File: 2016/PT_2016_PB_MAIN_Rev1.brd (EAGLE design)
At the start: 150.9 x 201.9 mm, 137 parts, among them M1+ ANDERSON_POWERPOLEPP45_PCB_HO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, M1- ANDERSON_POWERPOLEPP45_PCB_HO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, M2+ ANDERSON_POWERPOLEPP45_PCB_HO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, M2- ANDERSON_POWERPOLEPP45_PCB_HO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, M3+ ANDERSON_POWERPOLEPP45_PCB_HO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, M3- ANDERSON_POWERPOLEPP45_PCB_HO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, M4+ ANDERSON_POWERPOLEPP45_PCB_HO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, M4- ANDERSON_POWERPOLEPP45_PCB_HO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, M5+ ANDERSON_POWERPOLEPP45_PCB_HO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, M5- ANDERSON_POWERPOLEPP45_PCB_HO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, M6+ ANDERSON_POWERPOLEPP45_PCB_HO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, M6- ANDERSON_POWERPOLEPP45_PCB_HO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, Q1 Q_IRFS7437PbF, Q11 Q_IRFS7437PbF, Q12 2N7002, Q14 Q_IRFS7437PbF, Q16 Q_IRFS7437PbF, Q2 2N7002, Q20 Q_IRFS7437PbF, Q6 Q_IRFS7437PbF, Q7 Q_IRFS7437PbF, Q9 Q_IRFS7437PbF

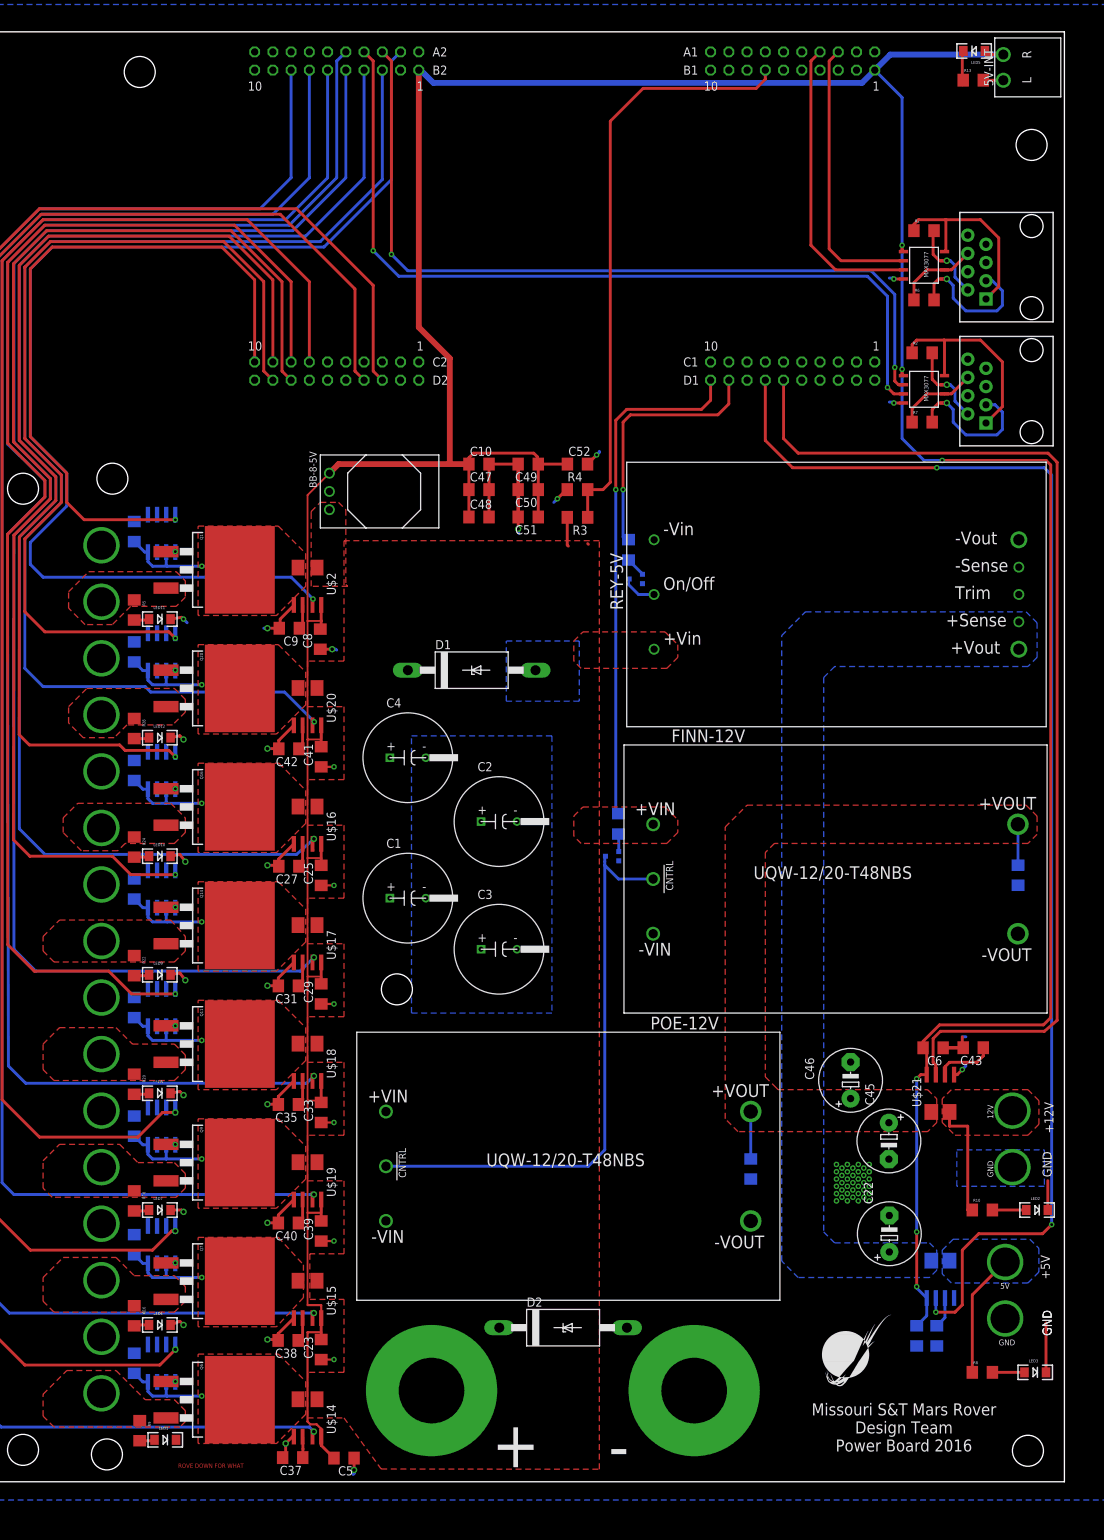
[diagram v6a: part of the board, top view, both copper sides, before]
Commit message: Final Power Board 2016 Rev 1
finalized routing, tplace labels, gnd return routes/vias
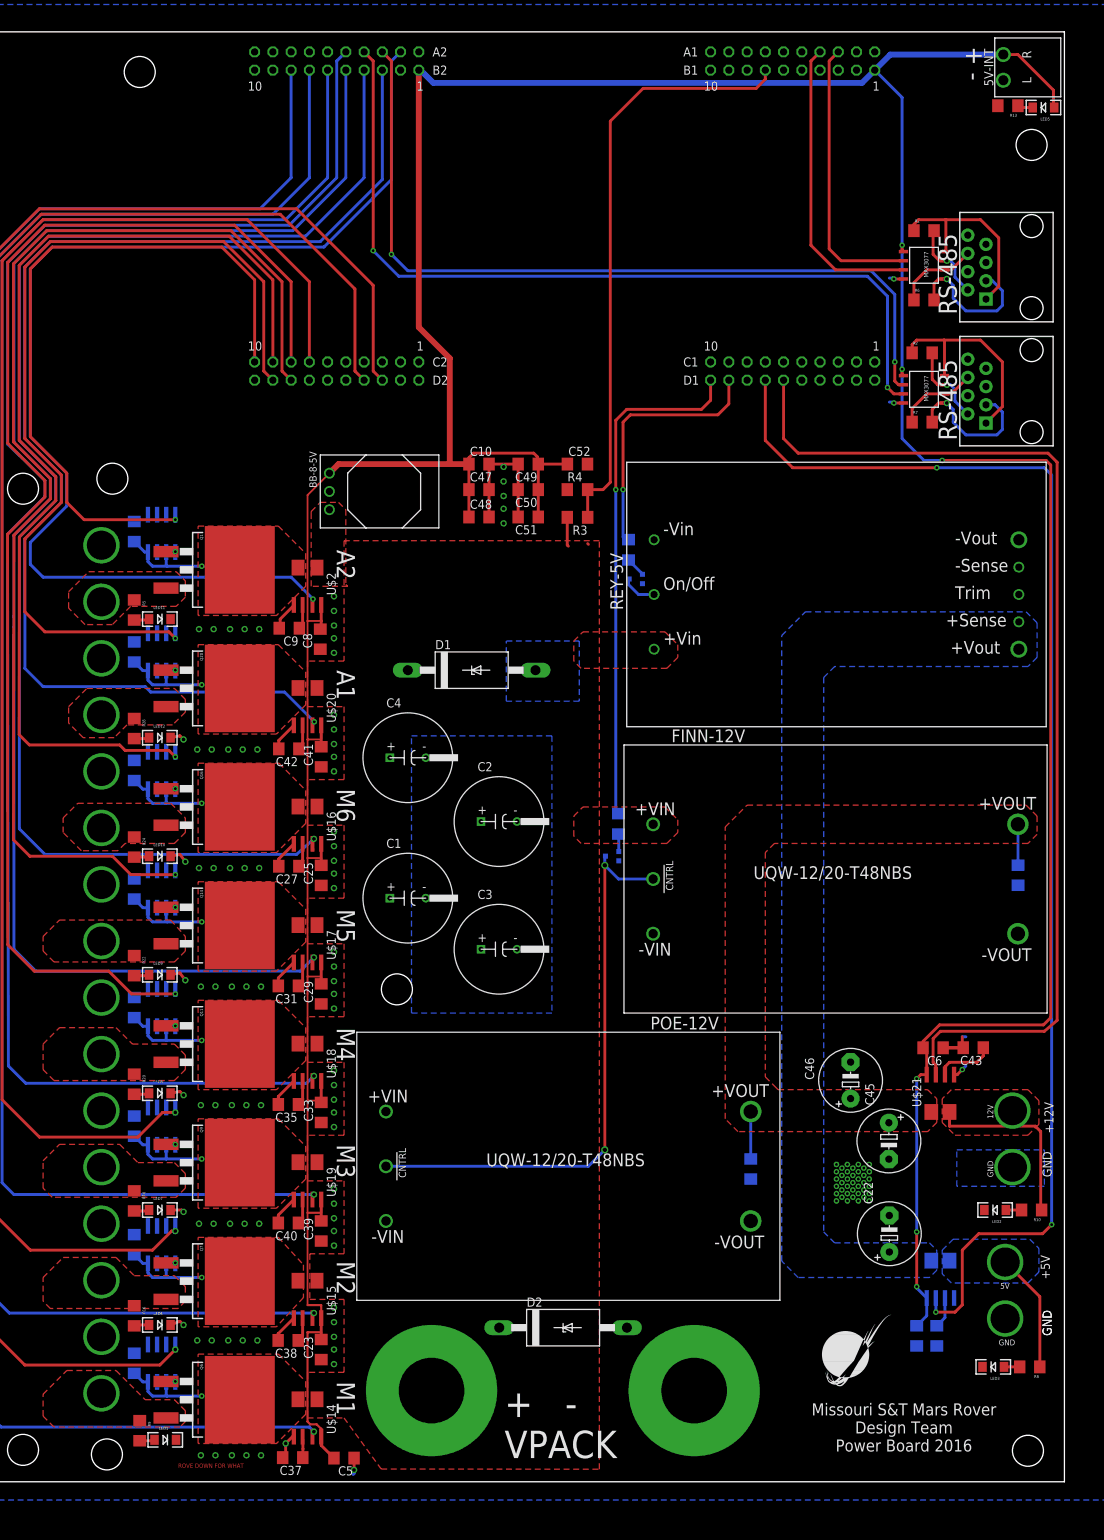
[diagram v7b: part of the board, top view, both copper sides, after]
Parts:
- moved LED5 12.5 mm to (143.1, 187.6)
- moved R10 6.86 mm to (141.5, 34.0), turned to 180 degrees
- moved R8 6.65 mm to (141.2, 12.2), turned to 180 degrees
- moved R13 5.99 mm to (138.2, 187.8), turned to 180 degrees
- moved LED3 5.89 mm to (136.1, 12.2), turned to 180 degrees
- moved LED2 5.84 mm to (136.4, 34.0), turned to 180 degrees
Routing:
- net GND: track 136.2 -> 80.6 mm, vias 68 -> 130
- net 12V-AUX: track 16.8 -> 26.0 mm
- net +5V: track 592.4 -> 600.6 mm
- net N$6: track 5.45 -> 2.16 mm
- net N$46: track 4.72 -> 2.18 mm
- net N$34: track 4.47 -> 2.18 mm
- net 5V-AUX: track 17.3 -> 16.6 mm
- net N$4: vias 0 -> 2
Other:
- board text added: "+ -"
- board text added: "+ - VPACK"
- board text added: "A1"
- board text added: "A2"
- board text added: "M1"
- board text added: "M2"
- board text added: "M3"
- board text added: "M4"
- board text added: "M5"
- board text added: "M6"
- board text added: "RS-485"
- board text removed: "+"
- board text removed: "-"

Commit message: gen gerbers for rev 1
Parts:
- moved U$45 0.25 mm to (134.1, 14.2)
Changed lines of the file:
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@@
 <layer number="16" name="Bottom" color="1" fill="1" visible="yes" active="yes"/>
 <layer number="17" name="Pads" color="2" fill="1" visible="yes" active="yes"/>
-<layer number="18" name="Vias" color="2" fill="1" visible="no" active="yes"/>
-<layer number="19" name="Unrouted" color="6" fill="1" visible="no" active="yes"/>
-<layer number="20" name="Dimension" color="15" fill="1" visible="no" active="yes"/>
+<layer number="18" name="Vias" color="2" fill="1" visible="yes" active="yes"/>
+<layer number="19" name="Unrouted" color="6" fill="1" visible="yes" active="yes"/>
+<layer number="20" name="Dimension" color="15" fill="1" visible="yes" active="yes"/>
 <layer number="21" name="tPlace" color="7" fill="1" visible="yes" active="yes"/>
-<layer number="22" name="bPlace" color="7" fill="1" visible="no" active="yes"/>
-<layer number="23" name="tOrigins" color="15" fill="1" visible="no" active="yes"/>
-<layer number="24" name="bOrigins" color="15" fill="1" visible="no" active="yes"/>
+<layer number="22" name="bPlace" color="7" fill="1" visible="yes" active="yes"/>
+<layer number="23" name="tOrigins" color="15" fill="1" visible="yes" active="yes"/>
+<layer number="24" name="bOrigins" color="15" fill="1" visible="yes" active="yes"/>
 <layer number="25" name="tNames" color="7" fill="1" visible="no" active="yes"/>
 <layer number="26" name="bNames" color="7" fill="1" visible="no" active="yes"/>
@@
 <layer number="47" name="Measures" color="7" fill="1" visible="no" active="yes"/>
 <layer number="48" name="Document" color="7" fill="1" visible="no" active="yes"/>
-<layer number="49" name="Reference" color="7" fill="1" visible="yes" active="yes"/>
+<layer number="49" name="Reference" color="7" fill="1" visible="no" active="yes"/>
 <layer number="50" name="dxf" color="7" fill="1" visible="no" active="yes"/>
-<layer number="51" name="tDocu" color="7" fill="1" visible="no" active="yes"/>
-<layer number="52" name="bDocu" color="7" fill="1" visible="no" active="yes"/>
+<layer number="51" name="tDocu" color="7" fill="1" visible="yes" active="yes"/>
+<layer number="52" name="bDocu" color="7" fill="1" visible="yes" active="yes"/>
 <layer number="91" name="Nets" color="2" fill="1" visible="no" active="no"/>
 <layer number="92" name="Busses" color="1" fill="1" visible="no" active="no"/>
@@
 <attribute name="COLOR1" value="" x="-16.256" y="4.572" size="1.778" layer="27" display="off"/>
 </element>
-<element name="U$45" library="MRDT-Connectors" package="APP_5V_VERT_CONFIG" value="APP_2POS_CONFIG5V_VERT" x="133.858" y="14.224">
-<attribute name="COLOR2" value="BLACK" x="133.858" y="14.224" size="1.778" layer="27" display="off"/>
-<attribute name="COLOR1" value="RED" x="133.858" y="14.224" size="1.778" layer="27" display="off"/>
+<element name="U$45" library="MRDT-Connectors" package="APP_5V_VERT_CONFIG" value="APP_2POS_CONFIG5V_VERT" x="134.112" y="14.224">
+<attribute name="COLOR2" value="BLACK" x="134.112" y="14.224" size="1.778" layer="27" display="off"/>
+<attribute name="COLOR1" value="RED" x="134.112" y="14.224" size="1.778" layer="27" display="off"/>
 </element>
 <element name="U$46" library="MRDT-Connectors" package="APP_12V_VERT_CONFIG" value="APP_2POS_CONFIG12V_VERT" x="134.112" y="36.068">
@@
 </polygon>
 <contactref element="U$45" pad="VCC"/>
-<wire x1="142.624" y1="12.192" x2="142.624" y2="21.968" width="0.4064" layer="1"/>
-<wire x1="142.624" y1="21.968" x2="137.795" y2="26.797" width="0.4064" layer="1"/>
+<wire x1="142.624" y1="12.192" x2="142.624" y2="22.222" width="0.4064" layer="1"/>
+<wire x1="142.624" y1="22.222" x2="138.049" y2="26.797" width="0.4064" layer="1"/>
 </signal>
 <signal name="N$35">
